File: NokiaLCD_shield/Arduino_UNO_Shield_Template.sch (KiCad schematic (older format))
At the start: 12 parts, among them CON1 Nokia1616_LCD, CON2 Micro_SD_Card, P1 CONN_01X02, Q1 BC548, U1 ArduinoUnoR3

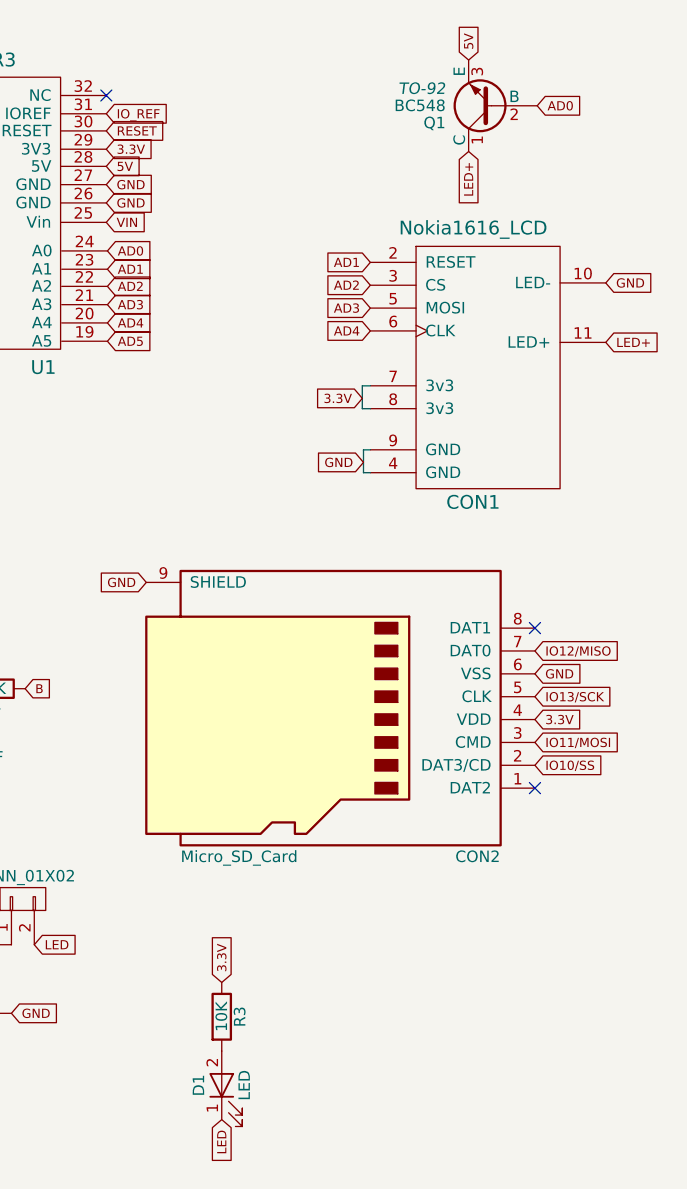
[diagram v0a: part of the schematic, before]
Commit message: Add arduino flex-sensor and SW2812B LED shields Add a folder for a flex-snsor arduino shield Add a folder for SW2812B LEDs arduino shield with a 4-channel 5v-3.3v levelshifter
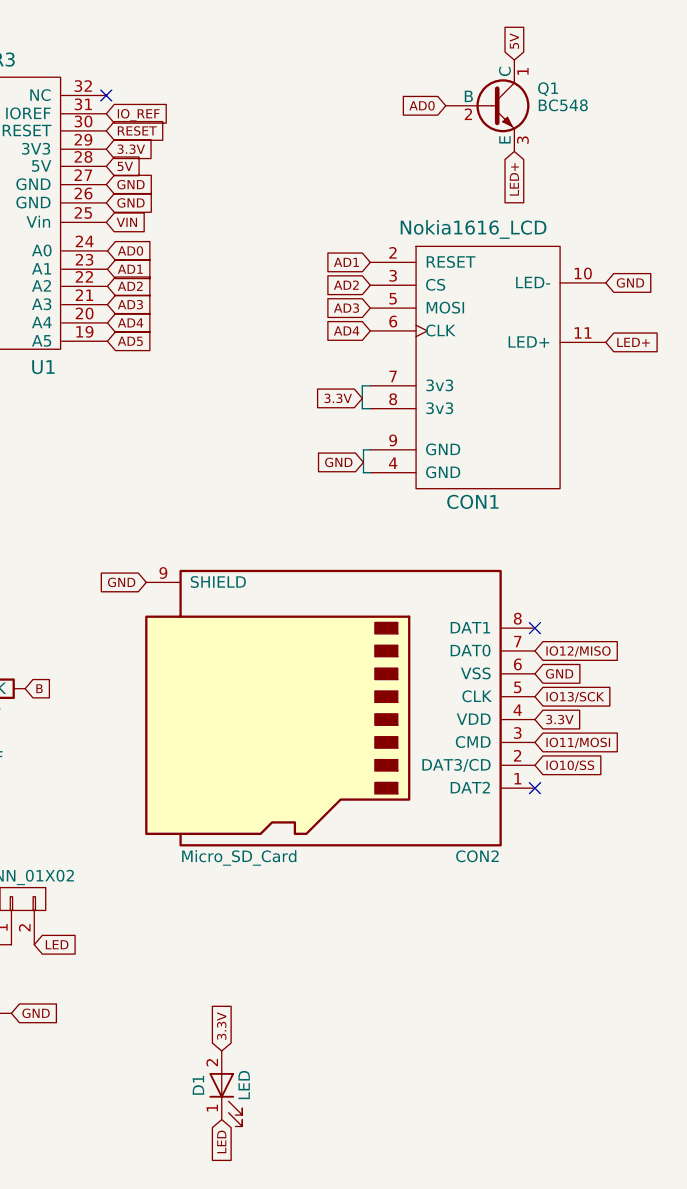
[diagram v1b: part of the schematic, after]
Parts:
- removed R3: 10K, Resistors_SMD:R_1206, symbol R
- CON2: footprint Connect:micro-SDcard -> Connect:MicroSDcard
- D1: footprint Resistors_SMD:R_1206 -> Resistors_SMD:R_0603
- Q1: footprint TO-92 -> TO_SOT_Packages_SMD:SOT-23
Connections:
- net 3.3V: now also D1.2 (A)
- net 5V: now also Q1.1 (C); no longer Q1.3 (E)
- net LED+: now also Q1.3 (E); no longer Q1.1 (C)
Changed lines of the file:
@@
 	1    0    0    -1
 $EndComp
-Text GLabel 4110 1020 1    40   Input ~ 0
+Text GLabel 4310 1020 1    40   Input ~ 0
 5V
 Text GLabel 3645 2500 0    40   Input ~ 0
@@
 F 0 "CON2" H 2850 4505 50  0000 C CNN
 F 1 "Micro_SD_Card" H 4150 4505 50  0000 R CNN
-F 2 "Connect:micro-SDcard" H 4650 4205 50  0001 C CNN
+F 2 "Connect:MicroSDcard" H 4650 4205 50  0001 C CNN
 F 3 "" H 3500 3905 50  0000 C CNN
 	1    3500 3905
 	-1   0    0    1
 $EndComp
-Text GLabel 4110 1420 3    40   Input ~ 0
+Text GLabel 4310 1420 3    40   Input ~ 0
 LED+
 Text GLabel 4710 2255 2    40   Input ~ 0
@@
 F 0 "Q1" H 4410 1295 50  0000 L CNN
 F 1 "BC548" H 4410 1220 50  0000 L CNN
-F 2 "TO-92" H 4410 1145 50  0000 L CIN
+F 2 "TO_SOT_Packages_SMD:SOT-23" H 4410 1145 50  0001 L CIN
 F 3 "" H 4210 1220 50  0000 L CNN
 	1    4210 1220
-	-1   0    0    1
+	1    0    0    -1
 $EndComp
 $Comp
@@
 Text GLabel 1305 2025 0    40   Input ~ 0
 IO7
-Text GLabel 4410 1220 2    40   Input ~ 0
+Text GLabel 4010 1220 0    40   Input ~ 0
 AD0
 Text GLabel 3680 1905 0    40   Input ~ 0
@@
 	930  3830 930  3780
 Connection ~ 930  3780
-Text GLabel 3030 5055 1    40   Input ~ 0
-3.3V
-$Comp
-L R R3
-U 1 1 5892BB4E
-P 3030 5205
-F 0 "R3" V 3110 5205 50  0000 C CNN
-F 1 "10K" V 3030 5205 50  0000 C CNN
-F 2 "Resistors_SMD:R_1206" V 2960 5205 50  0001 C CNN
-F 3 "" H 3030 5205 50  0000 C CNN
-	1    3030 5205
-	1    0    0    -1
-$EndComp
+Text GLabel 3030 5355 1    40   Input ~ 0
+3.3V
 Wire Wire Line
 	1815 3820 1815 3770
@@
 F 0 "D1" H 3030 5605 50  0000 C CNN
 F 1 "LED" H 3030 5405 50  0000 C CNN
-F 2 "Resistors_SMD:R_1206" H 3030 5505 50  0001 C CNN
+F 2 "Resistors_SMD:R_0603" H 3030 5505 50  0001 C CNN
 F 3 "" H 3030 5505 50  0000 C CNN
 	1    3030 5505

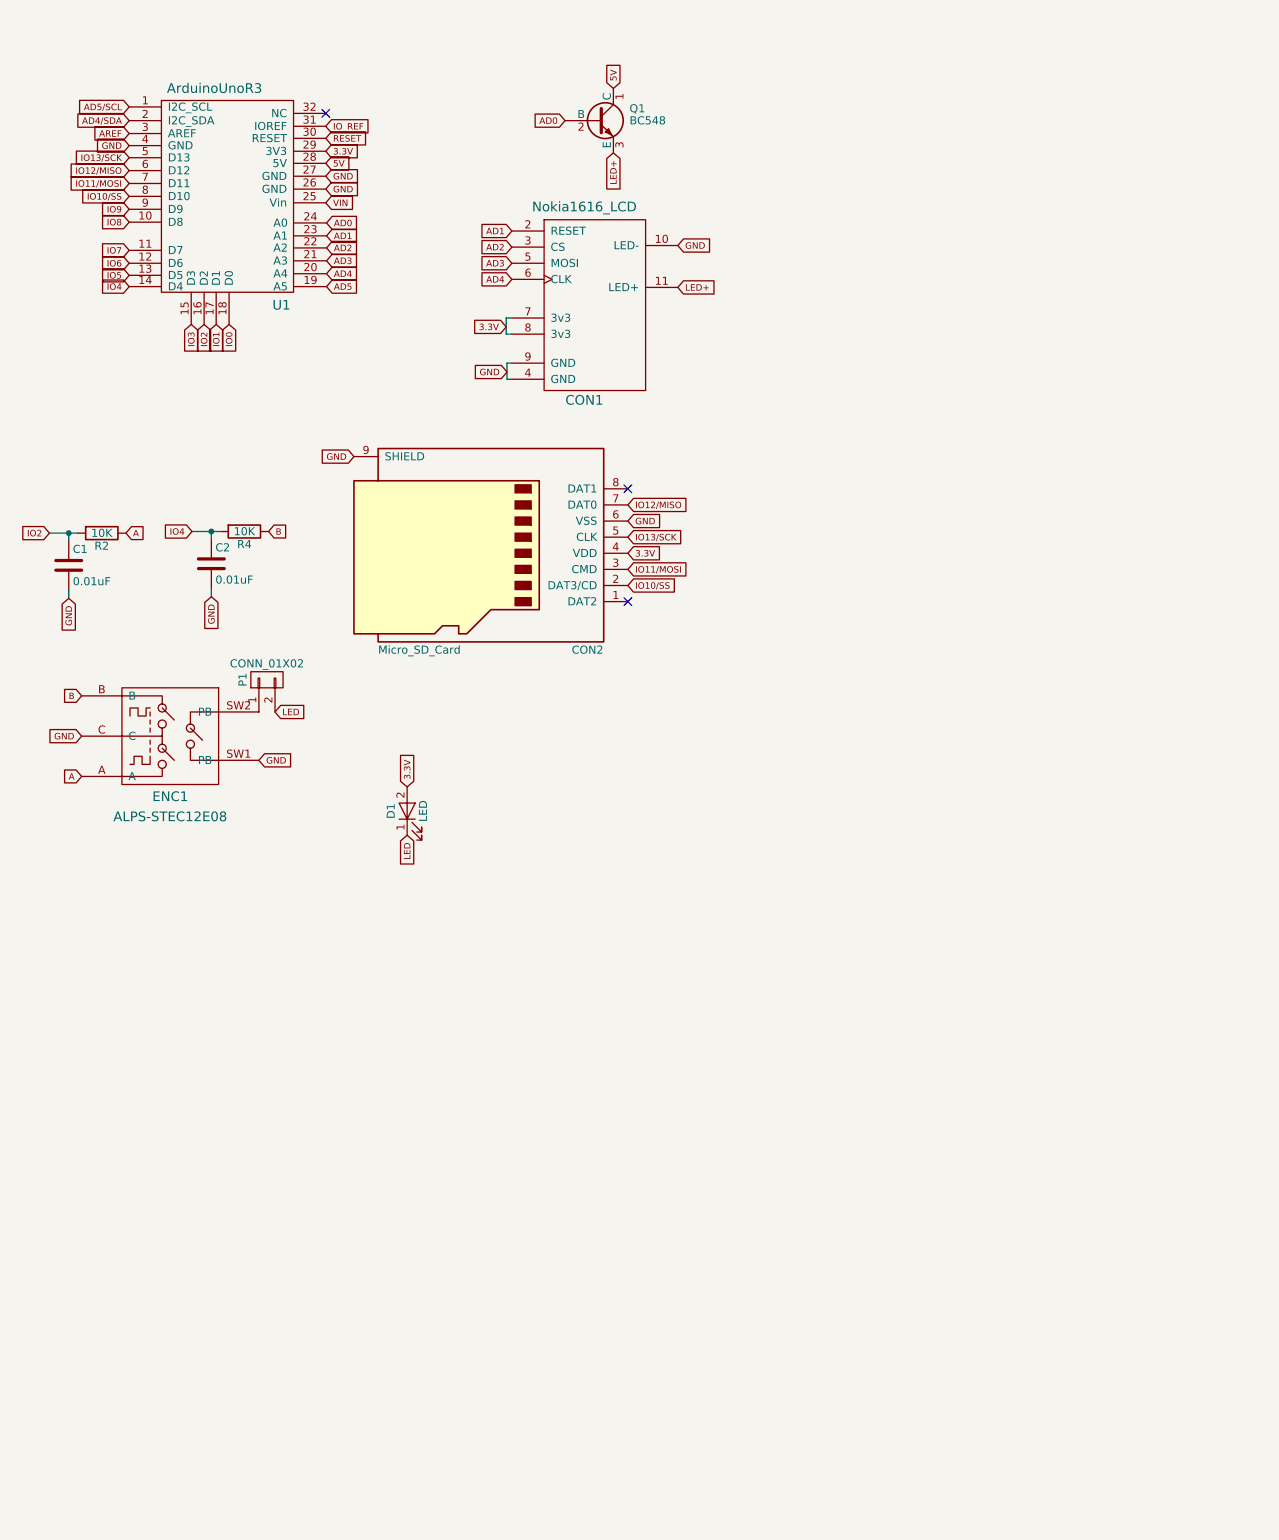
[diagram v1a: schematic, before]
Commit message: Changed Nokia1616 LCD backlight Added a low switch NPN transistor for PWM switching of backlight to ground Added a capacitor to ground on the 3v3 line Cleaned up the traces a bit
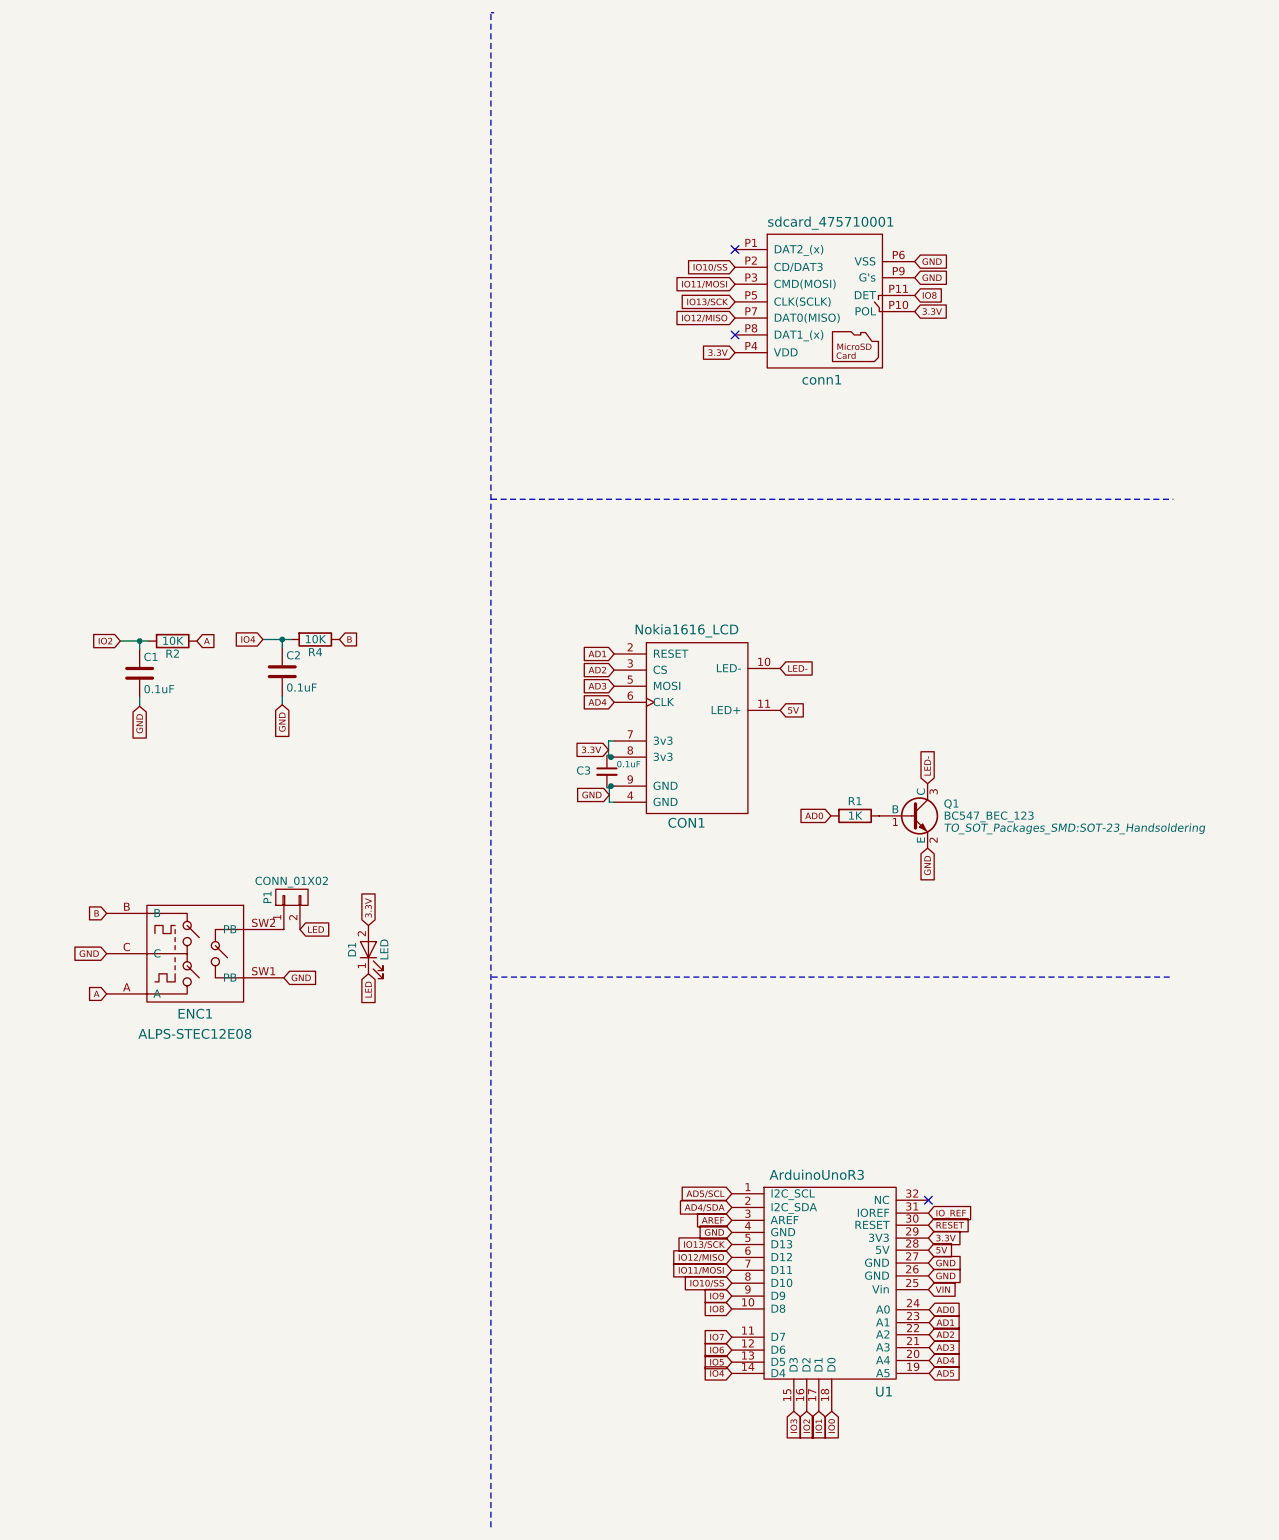
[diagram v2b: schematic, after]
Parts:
- removed CON2: Micro_SD_Card, Connect:MicroSDcard, symbol Micro_SD_Card
- removed Q1: BC548, TO_SOT_Packages_SMD:SOT-23, symbol BC548
- added C3: 0.1uF, Capacitors_SMD:C_1206, symbol C_Small
- added Q1: BC547_BEC_123, TO_SOT_Packages_SMD:SOT-23_Handsoldering, symbol BC547_BEC_123
- added R1: 1K, Resistors_SMD:R_1206, symbol R
- added conn1: sdcard_475710001, Connect:MicroSDcard-475710001, symbol sdcard_475710001
- C1, C2: value 0.01uF -> 0.1uF
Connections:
- net LED+ is gone; now on net 5V: CON1.11 (LED+)
- net 3.3V: now also C3.1, conn1.P10 (POL), conn1.P4 (VDD)
- net AD0: now also R1.2
- net GND: now also C3.2, Q1.2 (E), conn1.P6 (VSS), conn1.P9 (G's); no longer CON1.10 (LED-)
- net IO10/SS: now also conn1.P2 (CD/DAT3)
- net IO11/MOSI: now also conn1.P3 (CMD(MOSI))
- net IO12/MISO: now also conn1.P7 (DAT0(MISO))
- net IO13/SCK: now also conn1.P5 (CLK(SCLK))
- net IO8: now also conn1.P11 (DET)
- new net: Q1.1 (B), R1.1
- new net LED-: CON1.10 (LED-), Q1.3 (C)
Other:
- moved on the sheet: C1, C2, CON1, D1, ENC1, P1, R2, R4, U1
